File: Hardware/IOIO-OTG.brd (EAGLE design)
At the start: 68.6 x 30.5 mm, 54 parts, among them Q1 IRLML2244, Q2 MOSFET-NCHANNEL2N7002PW", U1 PIC24FJ256GB206, U14 SWITCH_SPDT, U2 TPS6214X"", U3 VREG_MIC5216

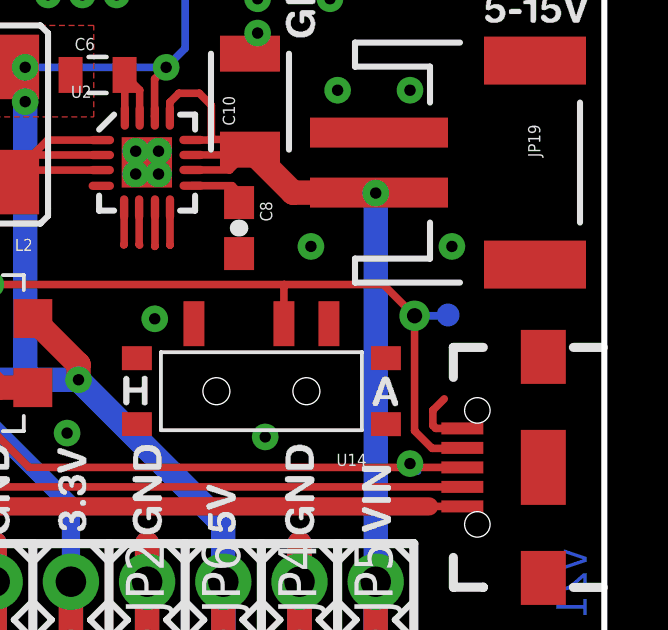
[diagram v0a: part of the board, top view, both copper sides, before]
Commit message: Slight test-point position change
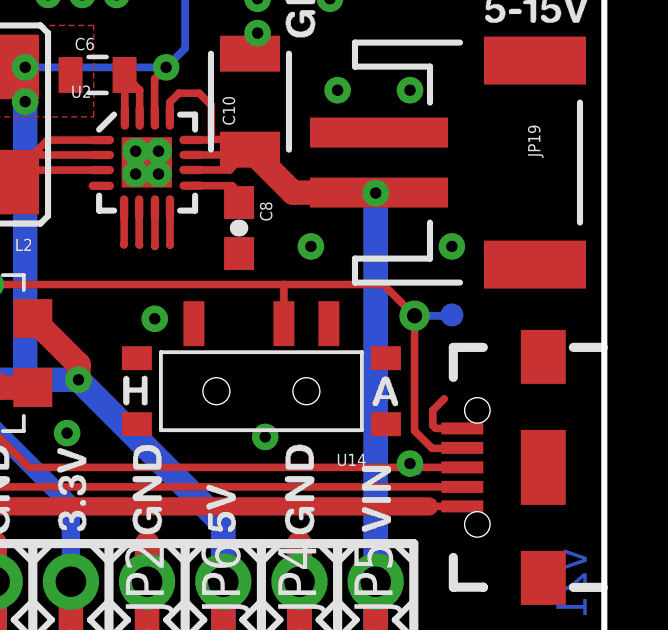
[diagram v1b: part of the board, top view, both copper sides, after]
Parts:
- moved TP4 0.13 mm to (63.5, 15.2), turned to 180 degrees
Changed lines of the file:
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@@
 <?xml version="1.0" encoding="utf-8"?>
 <!DOCTYPE eagle SYSTEM "eagle.dtd">
-<eagle version="6.5.0">
+<eagle version="6.4">
 <drawing>
 <settings>
@@
 <element name="TP2" library="SparkFun-Passives" package="PAD.03X.03" value="TEST-POINT3" x="41.91" y="6.35" rot="MR0"/>
 <element name="TP3" library="SparkFun-Passives" package="PAD.03X.03" value="TEST-POINT3" x="39.37" y="6.35" rot="MR0"/>
-<element name="TP4" library="SparkFun-Passives" package="PAD.03X.03" value="TEST-POINT3" x="63.373" y="15.24" rot="MR0"/>
+<element name="TP4" library="SparkFun-Passives" package="PAD.03X.03" value="TEST-POINT3" x="63.5" y="15.24" rot="MR180"/>
 </elements>
 <signals>
@@
 <via x="62.2554" y="15.2146" extent="1-16" drill="0.508"/>
 <wire x1="62.2554" y1="15.2146" x2="63.3476" y2="15.2146" width="0.254" layer="16"/>
-<wire x1="63.3476" y1="15.2146" x2="63.373" y2="15.24" width="0.254" layer="16"/>
+<wire x1="63.3476" y1="15.2146" x2="63.5" y2="15.24" width="0.254" layer="16"/>
 </signal>
 <signal name="VBUS">

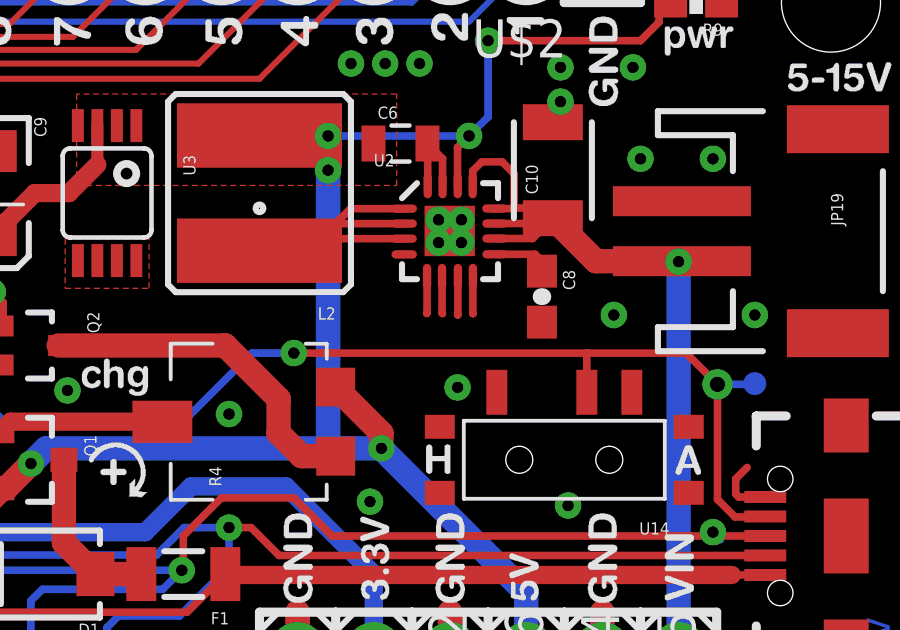
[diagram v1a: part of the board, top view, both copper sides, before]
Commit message: Added vias below TPS IC for better GND flow
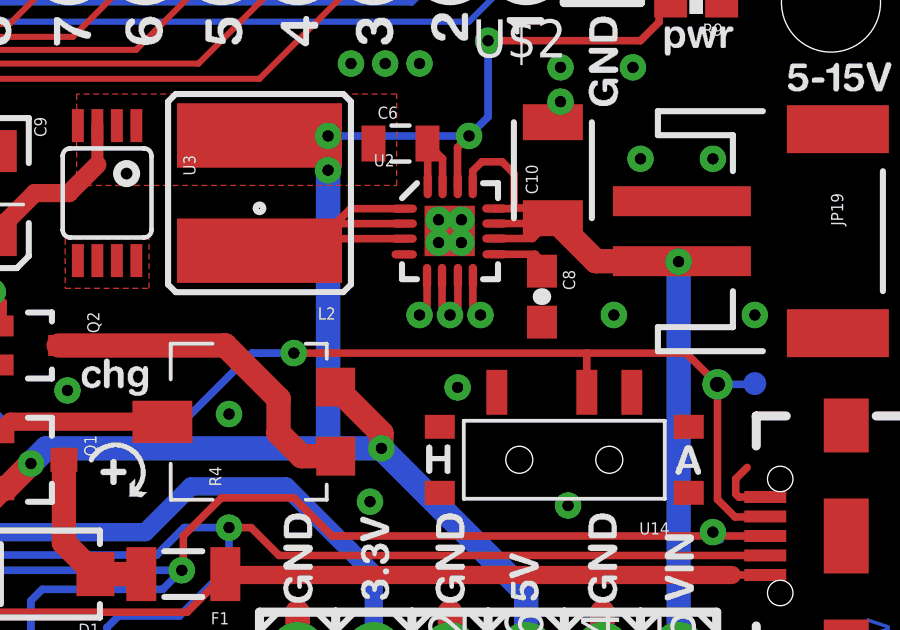
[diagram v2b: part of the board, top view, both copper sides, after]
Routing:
- net GND: vias 26 -> 29
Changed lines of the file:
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@@
 <wire x1="53.092540625" y1="22.737459375" x2="52.589" y2="23.241" width="0.254" layer="1"/>
 <contactref element="Q2" pad="2"/>
+<via x="52.324" y="17.526" extent="1-16" drill="0.381" diameter="0.889"/>
+<via x="53.34" y="17.526" extent="1-16" drill="0.381" diameter="0.889"/>
+<via x="54.356" y="17.526" extent="1-16" drill="0.381" diameter="0.889"/>
+<wire x1="54.356" y1="17.526" x2="54.104540625" y2="17.56918125" width="0" layer="19" extent="1-1"/>
+<wire x1="53.602703125" y1="18.8069" x2="54.1027" y2="18.8069" width="0" layer="19" extent="1-1"/>
+<wire x1="53.34" y1="17.526" x2="53.594" y2="17.526" width="0" layer="19" extent="1-1"/>
 </signal>
 <signal name="P7">

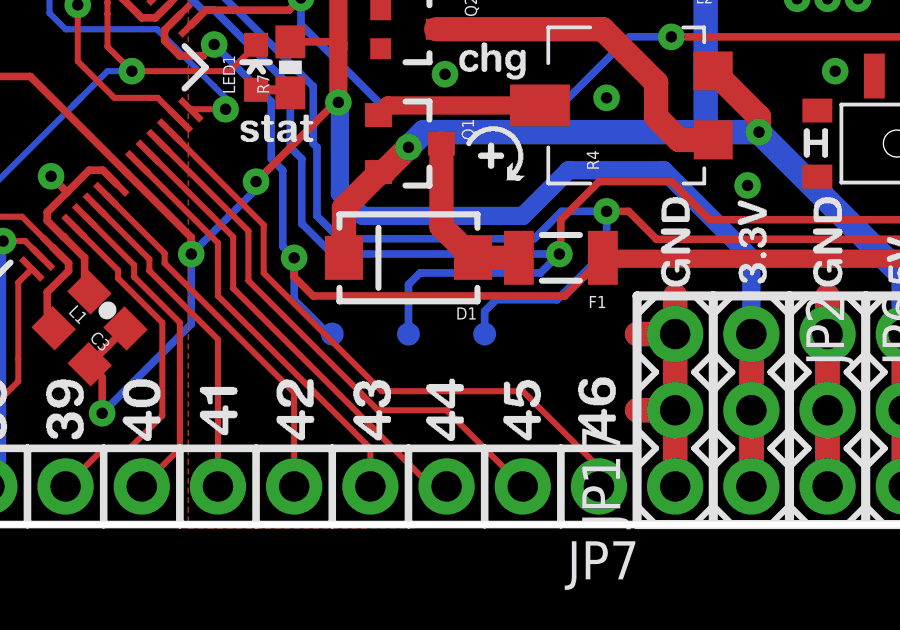
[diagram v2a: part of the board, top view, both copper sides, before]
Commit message: Changed positions of Test-Points
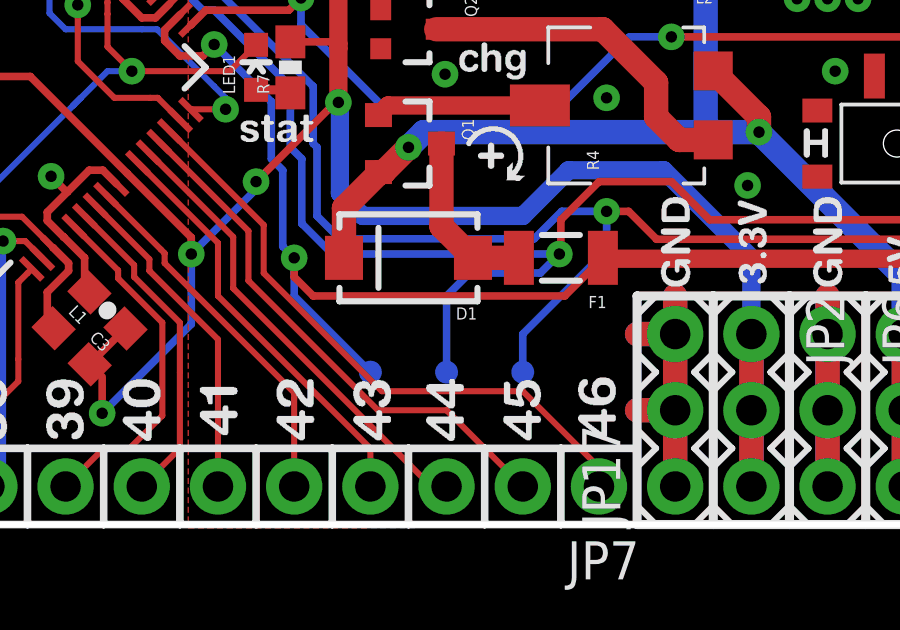
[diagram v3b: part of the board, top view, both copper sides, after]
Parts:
- moved TP1 1.80 mm to (38.1, 5.08)
- moved TP2 1.80 mm to (43.2, 5.08)
- moved TP3 1.80 mm to (40.6, 5.08)
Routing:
- net VBUS: track 44.2 -> 45.9 mm
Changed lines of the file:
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@@
 <rectangle x1="40.64" y1="23.1902" x2="43.18" y2="24.4856" layer="29"/>
 <rectangle x1="40.64" y1="18.6944" x2="43.18" y2="19.9898" layer="29"/>
-<text x="35.941" y="7.747" size="0.8128" layer="22" font="vector" ratio="15" rot="SMR270">VBUS</text>
-<text x="41.021" y="6.858" size="0.8128" layer="22" font="vector" ratio="15" rot="SMR270">D-</text>
-<text x="38.481" y="6.858" size="0.8128" layer="22" font="vector" ratio="15" rot="SMR270">D+</text>
+<text x="39.497" y="5.588" size="0.8128" layer="22" font="vector" ratio="15" rot="MR0">VBUS</text>
+<text x="42.418" y="6.477" size="0.8128" layer="22" font="vector" ratio="15" rot="MR180">D-</text>
+<text x="39.878" y="6.477" size="0.8128" layer="22" font="vector" ratio="15" rot="MR180">D+</text>
 <text x="63.754" y="14.478" size="0.8128" layer="22" font="vector" ratio="15" rot="SMR270">ID</text>
 </plain>
@@
 <element name="U4" library="Testing" package="USB-AB-MICRO-SMD_V03" value="" x="66.548" y="10.16" rot="R180"/>
 <element name="U2" library="SparkFun-PowerIC" package="QFN16-3X3MM_1:1_V03" value="TPS6214X&quot;&quot;" x="53.34" y="20.32"/>
-<element name="TP1" library="SparkFun-Passives" package="PAD.03X.03" value="TEST-POINT3" x="36.83" y="6.35" rot="MR0"/>
+<element name="TP1" library="SparkFun-Passives" package="PAD.03X.03" value="TEST-POINT3" x="38.1" y="5.08" rot="MR0"/>
 <element name="C9" library="SparkFun-Capacitors" package="EIA3216" value="10uf" x="38.1" y="21.59" rot="R270"/>
 <element name="C10" library="SparkFun-Passives" package="1210" value="10uf" x="56.769" y="22.352" rot="R90"/>
@@
 <element name="Q2" library="SparkFun-DiscreteSemi" package="SOT323_NOAT" value="MOSFET-NCHANNEL2N7002PW&quot;" x="39.37" y="16.51" rot="R270"/>
 <element name="R4" library="Testing" package="TRIMPOT_5MM" value="TRIMPOTSMD_STANDARD" x="46.99" y="13.97" rot="R90"/>
-<element name="TP2" library="SparkFun-Passives" package="PAD.03X.03" value="TEST-POINT3" x="41.91" y="6.35" rot="MR0"/>
-<element name="TP3" library="SparkFun-Passives" package="PAD.03X.03" value="TEST-POINT3" x="39.37" y="6.35" rot="MR0"/>
+<element name="TP2" library="SparkFun-Passives" package="PAD.03X.03" value="TEST-POINT3" x="43.18" y="5.08" rot="MR0"/>
+<element name="TP3" library="SparkFun-Passives" package="PAD.03X.03" value="TEST-POINT3" x="40.64" y="5.08" rot="MR0"/>
 <element name="TP4" library="SparkFun-Passives" package="PAD.03X.03" value="TEST-POINT3" x="63.5" y="15.24" rot="MR180"/>
 </elements>
@@
 <via x="53.34" y="17.526" extent="1-16" drill="0.381" diameter="0.889"/>
 <via x="54.356" y="17.526" extent="1-16" drill="0.381" diameter="0.889"/>
-<wire x1="54.356" y1="17.526" x2="54.104540625" y2="17.56918125" width="0" layer="19" extent="1-1"/>
-<wire x1="53.602703125" y1="18.8069" x2="54.1027" y2="18.8069" width="0" layer="19" extent="1-1"/>
-<wire x1="53.34" y1="17.526" x2="53.594" y2="17.526" width="0" layer="19" extent="1-1"/>
 </signal>
 <signal name="P7">
@@
 <wire x1="47.64" y1="9.51" x2="63.848" y2="9.51" width="0.254" layer="1"/>
 <contactref element="TP2" pad="P$1"/>
-<wire x1="41.91" y1="6.35" x2="41.91" y2="7.112" width="0.254" layer="16"/>
-<wire x1="41.91" y1="7.112" x2="42.291" y2="7.493" width="0.254" layer="16"/>
-<wire x1="42.291" y1="7.493" x2="44.323" y2="7.493" width="0.254" layer="16"/>
-<wire x1="44.323" y1="7.493" x2="45.974" y2="9.144" width="0.254" layer="16"/>
+<wire x1="43.18" y1="6.35" x2="45.974" y2="9.144" width="0.254" layer="16"/>
 <wire x1="45.974" y1="9.144" x2="45.974" y2="10.4394" width="0.254" layer="16"/>
+<wire x1="43.18" y1="5.08" x2="43.18" y2="6.35" width="0.254" layer="16"/>
 </signal>
 <signal name="D+">
@@
 <wire x1="62.23" y1="10.16" x2="62.103" y2="10.287" width="0.254" layer="1"/>
 <contactref element="TP3" pad="P$1"/>
-<wire x1="39.37" y1="6.35" x2="39.37" y2="8.001" width="0.254" layer="16"/>
-<wire x1="39.37" y1="8.001" x2="39.751" y2="8.382" width="0.254" layer="16"/>
-<wire x1="39.751" y1="8.382" x2="43.7642" y2="8.382" width="0.254" layer="16"/>
 <wire x1="43.7642" y1="8.382" x2="44.3992" y2="9.017" width="0.254" layer="16"/>
+<wire x1="40.64" y1="5.08" x2="40.64" y2="7.62" width="0.254" layer="16"/>
+<wire x1="40.64" y1="7.62" x2="41.402" y2="8.382" width="0.254" layer="16"/>
+<wire x1="41.402" y1="8.382" x2="43.7642" y2="8.382" width="0.254" layer="16"/>
 </signal>
 <signal name="VIN">
@@
 <wire x1="63.848" y1="8.86" x2="62.738" y2="8.86" width="0.254" layer="1"/>
 <contactref element="TP1" pad="P$1"/>
-<wire x1="35.5346" y1="8.8646" x2="35.56" y2="8.89" width="0.254" layer="16"/>
 <contactref element="F1" pad="1"/>
 <wire x1="44.58" y1="7.62" x2="45.85" y2="8.89" width="0.254" layer="1"/>
 <wire x1="45.88" y1="8.86" x2="45.85" y2="8.89" width="0.254" layer="1"/>
-<wire x1="36.83" y1="6.35" x2="36.703" y2="6.35" width="0.254" layer="16"/>
-<wire x1="36.703" y1="6.35" x2="35.56" y2="7.493" width="0.254" layer="16"/>
-<wire x1="35.56" y1="7.493" x2="35.56" y2="8.89" width="0.254" layer="16"/>
+<wire x1="38.1" y1="5.08" x2="35.56" y2="7.62" width="0.254" layer="16"/>
+<wire x1="35.56" y1="7.62" x2="35.56" y2="8.89" width="0.254" layer="16"/>
 </signal>
 <signal name="N$9">

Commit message: Adding in hardware changes from Pete
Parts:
- removed LED1: LY L29K-J1K2-26-Z, SparkFun-LED:LED-0603
- removed LED2: LS L29K-G1J2-1-Z, SparkFun:LED-0603
- removed TP4: TEST-POINT3, SparkFun-Passives:PAD.03X.03
- removed U$1: CREATIVE_COMMONS, SparkFun-Aesthetics:CREATIVE_COMMONS
- removed U14: SWITCH_SPDT, SparkFun-Electromechanical:KPS-1290
- removed U4: (no value), Testing:USB-AB-MICRO-SMD_V03
- added C11: 10uF, SparkFun-Capacitors:1210
- added D2: DZ2J160M0L, SparkFun-DiscreteSemi:PANASONIC_SMINI2-F5-B
- added D3: Yellow, SparkFun-LED:LED-0603
- added D5: Red, SparkFun-LED:LED-0603
- added FRAME2: FRAME-LEDGER, SparkFun-Aesthetics:CREATIVE_COMMONS
- added JP21: AB MICRO USB, SparkFun-Connectors:USB-AB-MICRO-SMD_V03
- added LOGO1: OSHW-LOGOS, SparkFun-Aesthetics:OSHW-LOGO-S
- added LOGO2: SFE_LOGO_NAME_FLAME.1_INCH, SparkFun-Aesthetics:SFE_LOGO_NAME_FLAME_.1
- added LOGO3: SFE_LOGO_FLAME.1_INCH, SparkFun-Aesthetics:SFE_LOGO_FLAME_.1
- added Q3: MOSFET-NCHANNELAO3404A, SparkFun-DiscreteSemi:SOT23-3
- added R3: TS53YL502MR10, SparkFun-Electromechanical:TRIMPOT_5MM
- added S1: SWITCH_SPDT, SparkFun-Electromechanical:KPS-1290
- C10: value 10uf -> 10uF; device SparkFun-Passives:1210 -> SparkFun-Capacitors:EIA3216
- C6: value 10uf -> 10uF; device SparkFun-Passives:0805 -> SparkFun-Capacitors:0805-CAP
- C7: device SparkFun:EIA3216 -> SparkFun-Capacitors:EIA3216
- C9: value 10uf -> 0.1uF; device SparkFun-Capacitors:EIA3216 -> SparkFun-Capacitors:0603-CAP
- D1: value DIODE-SCHOTTKY_ -> B340A
- F1: value PTCSMD -> 0.75A
- JP1: value VIN -> (none)
- JP14, JP15, JP3: value M01PTH -> (none)
- JP19: value JST Connector -> JST; device SparkFun:JST-2-SMD -> SparkFun-Connectors:JST-2-SMD
- JP20: value M191X19_NO_SILK -> (none)
- JP4: value 5V -> (none)
- JP7: value M161X16_NO_SILK -> (none)
- JP9: value M111X11_NO_SILK -> (none)
- Q2: value MOSFET-NCHANNEL2N7002PW" -> 2N7002PW; device SparkFun-DiscreteSemi:SOT323_NOAT -> SparkFun-DiscreteSemi:SOT323
- R1: value 10k -> 10K
- R4: value TRIMPOTSMD_STANDARD -> 3.3k; device Testing:TRIMPOT_5MM -> SparkFun-Resistors:0603-RES
- R9: value 1.6k -> 1.6K
- U2: value TPS6214X"" -> TPS62133RGTT
- U3: value VREG_MIC5216 -> MIC5216
- moved TP1 28.6 mm to (65.7, 12.6)
- moved TP3 25.2 mm to (65.7, 8.00)
- moved TP2 22.8 mm to (65.4, 10.3)
- moved C10 17.9 mm to (38.9, 23.1)
- moved C9 17.7 mm to (55.8, 20.5)
- moved R4 6.94 mm to (53.7, 15.6), turned to 180 degrees
- moved F1 5.32 mm to (48.5, 12.3)
- moved D1 4.04 mm to (42.2, 11.8)
- moved C5 2.97 mm to (31.9, 18.7)
- moved Q1 2.73 mm to (40.6, 15.1)
- moved C3 2.68 mm to (29.9, 9.75), turned to 315 degrees
- moved R2 2.68 mm to (29.4, 21.4)
- moved C4 2.65 mm to (17.7, 5.85), turned to 225 degrees
- moved C2 2.63 mm to (30.8, 20.7)
- moved C1 2.56 mm to (26.8, 6.63), turned to 315 degrees
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- renumbered U$2 to JP20
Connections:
- new net ANCHOR1: JP21.SHIELD1, JP21.SHIELD2, JP21.SHIELD3
- new net N$12: D2.A, Q3.1, R4.1
- net 3.3V: now also C10.A; no longer C9.A
- net 5V: now also R3.A; no longer R4.A
- net BOOT: now also D3.C; no longer LED1.C
- net D+: now also JP21.D+1, TP2.P$1; no longer TP3.P$1, U4.D+1
- net D-: now also JP21.D-1, TP3.P$1; no longer TP2.P$1, U4.D-1
- net GND: now also C10.C, C11.2, C9.2, D5.C, JP21.GND1, Q3.2, R4.2, S1.S; no longer C10.2, C9.C, LED2.C, U14.O, U4.GND1
- net N$1: now also R3.B; no longer R4.B
- net N$2: now also D3.A; no longer LED1.A
- net N$3: now also D5.A; no longer LED2.A
- net N$8: now also R3.C; no longer R4.C
- net USBID: now also JP21.ID1, S1.P, TP1.P$1; no longer TP4.P$1, U14.P, U4.ID1
- net VBUS: now also JP21.VBUS1; no longer TP1.P$1, U4.VBUS1
- net VIN: now also C11.1, C9.1, D2.C, Q3.3; no longer C10.1
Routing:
- net GND: track 74.9 -> 52.1 mm, vias 29 -> 82
- net BOOT: track 27.7 -> 38.1 mm
- net VIN: track 38.7 -> 28.5 mm
- net 3.3V: track 101.7 -> 111.4 mm, vias 4 -> 9
- net N$8: track 11.4 -> 3.58 mm
- net N$6: track 10.5 -> 3.14 mm
- net N$9: track 9.66 -> 3.63 mm
- net PIN31: track 24.8 -> 19.0 mm, vias 1 -> 0
- net N$1: track 5.51 -> 10.9 mm
- net PIN23: track 13.2 -> 18.5 mm
- net PIN10: track 12.0 -> 17.0 mm
- net PIN1: track 39.2 -> 44.0 mm
- net HOST: track 14.1 -> 18.6 mm
- net D-: track 46.3 -> 50.8 mm, vias 2 -> 1
- net PIN44: track 15.6 -> 19.8 mm
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- added copper zone on layer 1, net ANCHOR1
- added copper zone on layer 1, net N$6
- added copper zone on layer 1, net VIN
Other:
- board text added: "+"
- board text added: "Aaron Weiss, Pete Lewis"
- board text added: "Revised by:"
- board text added: "Units are in inches"
- board text added: "Ytai Ben-tsvi"
- board text added: "v22b"
- board text removed: "D+"
- board text removed: "D-"
- board text removed: "ID"
- board text removed: "VBUS"
- board text removed: "v21"
